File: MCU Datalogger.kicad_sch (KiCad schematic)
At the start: 0 parts

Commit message: Have added required symbols to the schematic sheets.
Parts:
- added BT?: Battery, symbol Device:Battery
- added C? (x4): C, symbol Device:C
- added C?: C_Polarized, symbol Device:C_Polarized
- added D? (x2): LED, symbol Device:LED
- added H? (x4): MountingHole, symbol Mechanical:MountingHole
- added R? (x7): R, symbol Device:R
- added U?: DS1337S+, SOIC127P600X175-8N, symbol DS1337S_:DS1337S+
- added U?: ATMEGA328P-AU, QFP80P900X900X120-32N, symbol ATMEGA328P-AU:ATMEGA328P-AU
- added U? (x2): 24LC1025, symbol Memory_EEPROM:24LC1025
- added Y? (x2): Crystal, symbol Device:Crystal
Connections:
- new net: U?.21 (GND), U?.3 (GND), U?.5 (GND)
- new net: U?.4 (VCC), U?.6 (VCC)
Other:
- added sheet Connectors (connectors.kicad_sch)

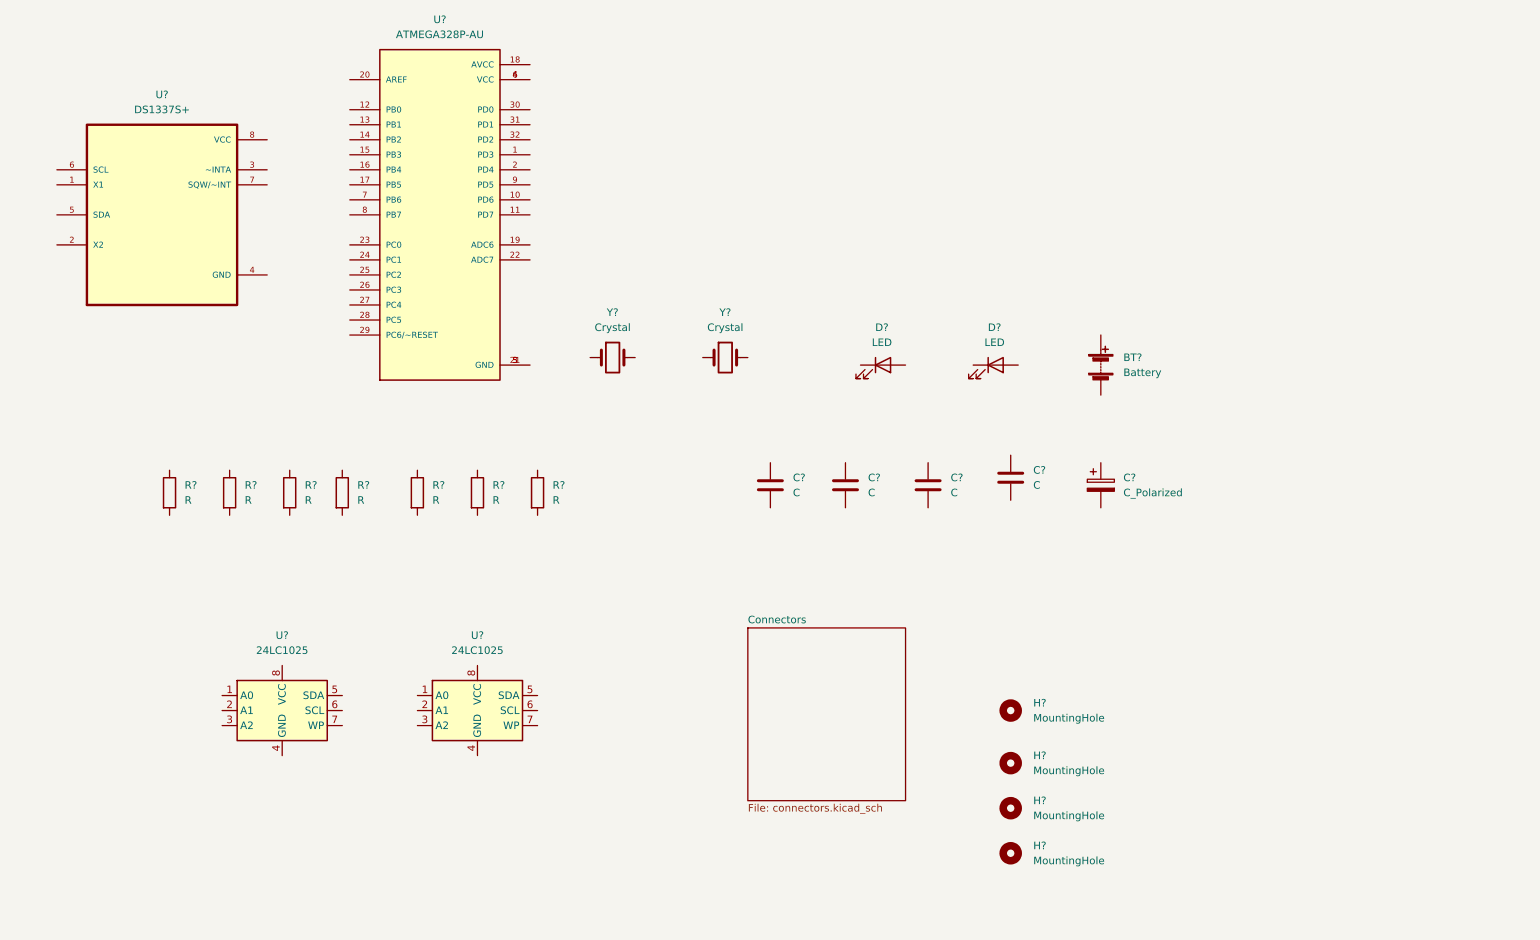
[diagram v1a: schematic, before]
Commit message: Changed locations of symbols (arrange).
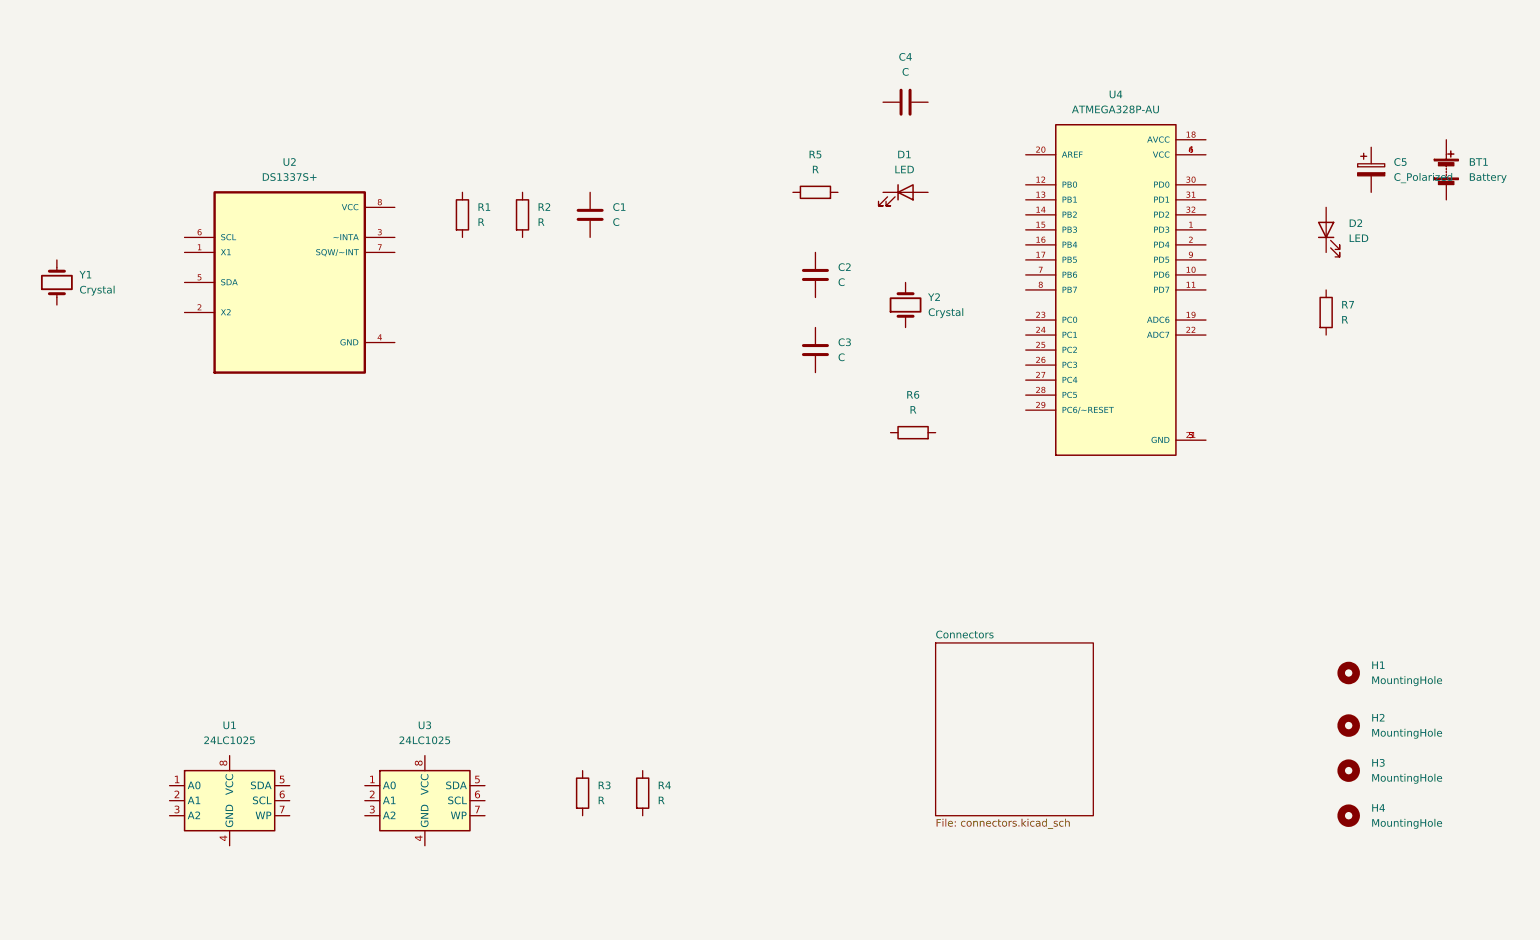
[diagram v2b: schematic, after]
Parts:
- gave numbers to parts that had none: 25
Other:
- moved on the sheet: BT1, C1, C2, C3, C4, C5, D1, D2, H1, H2, H3, H4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

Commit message: Added component values.
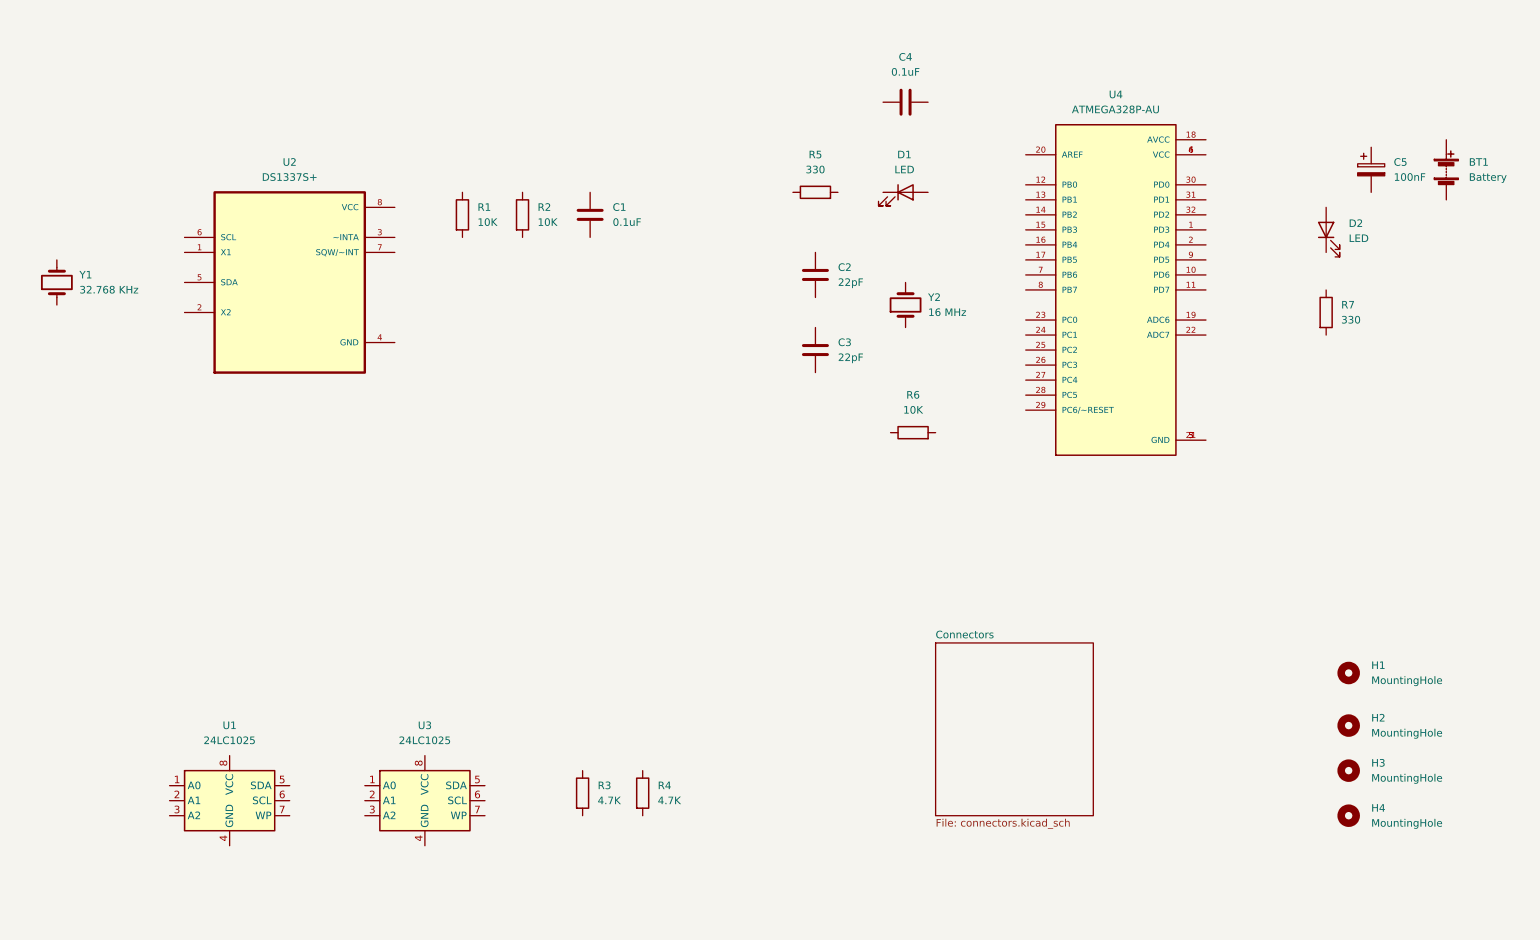
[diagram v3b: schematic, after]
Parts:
- C1, C4: value C -> 0.1uF
- C2, C3: value C -> 22pF
- C5: value C_Polarized -> 100nF
- R1, R2, R6: value R -> 10K
- R3, R4: value R -> 4.7K
- R5, R7: value R -> 330
- Y1: value Crystal -> 32.768 KHz
- Y2: value Crystal -> 16 MHz
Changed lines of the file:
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@@
       (effects (font (size 1.27 1.27)) (justify left))
     )
-    (property "Value" "R" (id 1) (at 99.06 52.0699 0)
+    (property "Value" "10K" (id 1) (at 99.06 52.0699 0)
       (effects (font (size 1.27 1.27)) (justify left))
     )
@@
       (effects (font (size 1.27 1.27)) (justify left))
     )
-    (property "Value" "R" (id 1) (at 109.22 52.0699 0)
+    (property "Value" "10K" (id 1) (at 109.22 52.0699 0)
       (effects (font (size 1.27 1.27)) (justify left))
     )
@@
       (effects (font (size 1.27 1.27)) (justify left))
     )
-    (property "Value" "R" (id 1) (at 119.38 149.8599 0)
+    (property "Value" "4.7K" (id 1) (at 119.38 149.8599 0)
       (effects (font (size 1.27 1.27)) (justify left))
     )
@@
       (effects (font (size 1.27 1.27)) (justify left))
     )
-    (property "Value" "R" (id 1) (at 129.54 149.8599 0)
+    (property "Value" "4.7K" (id 1) (at 129.54 149.8599 0)
       (effects (font (size 1.27 1.27)) (justify left))
     )
@@
     (in_bom yes) (on_board yes) (fields_autoplaced)
     (property "Reference" "R5" (id 0) (at 156.21 40.64 90))
-    (property "Value" "R" (id 1) (at 156.21 43.18 90))
+    (property "Value" "330" (id 1) (at 156.21 43.18 90))
     (property "Footprint" "" (id 2) (at 156.21 48.768 90)
       (effects (font (size 1.27 1.27)) hide)
@@
     (in_bom yes) (on_board yes) (fields_autoplaced)
     (property "Reference" "R6" (id 0) (at 172.72 81.28 90))
-    (property "Value" "R" (id 1) (at 172.72 83.82 90))
+    (property "Value" "10K" (id 1) (at 172.72 83.82 90))
     (property "Footprint" "" (id 2) (at 172.72 89.408 90)
       (effects (font (size 1.27 1.27)) hide)
@@
       (effects (font (size 1.27 1.27)) (justify left))
     )
-    (property "Value" "R" (id 1) (at 245.11 68.5799 0)
+    (property "Value" "330" (id 1) (at 245.11 68.5799 0)
       (effects (font (size 1.27 1.27)) (justify left))
     )
@@
       (effects (font (size 1.27 1.27)) (justify left))
     )
-    (property "Value" "C" (id 1) (at 121.92 52.0699 0)
+    (property "Value" "0.1uF" (id 1) (at 121.92 52.0699 0)
       (effects (font (size 1.27 1.27)) (justify left))
     )
@@
       (effects (font (size 1.27 1.27)) (justify left))
     )
-    (property "Value" "C" (id 1) (at 160.02 62.2299 0)
+    (property "Value" "22pF" (id 1) (at 160.02 62.2299 0)
       (effects (font (size 1.27 1.27)) (justify left))
     )
@@
       (effects (font (size 1.27 1.27)) (justify left))
     )
-    (property "Value" "C" (id 1) (at 160.02 74.9299 0)
+    (property "Value" "22pF" (id 1) (at 160.02 74.9299 0)
       (effects (font (size 1.27 1.27)) (justify left))
     )
@@
     (in_bom yes) (on_board yes) (fields_autoplaced)
     (property "Reference" "C4" (id 0) (at 171.45 24.13 90))
-    (property "Value" "C" (id 1) (at 171.45 26.67 90))
+    (property "Value" "0.1uF" (id 1) (at 171.45 26.67 90))
     (property "Footprint" "" (id 2) (at 175.26 30.7848 0)
       (effects (font (size 1.27 1.27)) hide)
@@
       (effects (font (size 1.27 1.27)) (justify left))
     )
-    (property "Value" "C_Polarized" (id 1) (at 254 44.4499 0)
+    (property "Value" "100nF" (id 1) (at 254 44.4499 0)
       (effects (font (size 1.27 1.27)) (justify left))
     )
@@
       (effects (font (size 1.27 1.27)) (justify right))
     )
-    (property "Value" "Crystal" (id 1) (at 31.75 63.4999 90)
+    (property "Value" "32.768 KHz" (id 1) (at 31.75 63.4999 90)
       (effects (font (size 1.27 1.27)) (justify right))
     )
@@
       (effects (font (size 1.27 1.27)) (justify right))
     )
-    (property "Value" "Crystal" (id 1) (at 175.26 67.3099 90)
+    (property "Value" "16 MHz" (id 1) (at 175.26 67.3099 90)
       (effects (font (size 1.27 1.27)) (justify right))
     )
@@
     )
     (path "/6297028a-be71-4f20-91c8-82bcaff02548"
-      (reference "C1") (unit 1) (value "C") (footprint "")
+      (reference "C1") (unit 1) (value "0.1uF") (footprint "")
     )
     (path "/b20b651d-5224-4b1d-8058-dedf55548381"
-      (reference "C2") (unit 1) (value "C") (footprint "")
+      (reference "C2") (unit 1) (value "22pF") (footprint "")
     )
     (path "/61e91196-d43d-4b19-ad57-2569feed4c9f"
-      (reference "C3") (unit 1) (value "C") (footprint "")
+      (reference "C3") (unit 1) (value "22pF") (footprint "")
     )
     (path "/e18320b2-42ab-4621-9e66-aee24e50ee4d"
-      (reference "C4") (unit 1) (value "C") (footprint "")
+      (reference "C4") (unit 1) (value "0.1uF") (footprint "")
     )
     (path "/9848e6a5-7312-4f8c-92b1-3add5171e047"
-      (reference "C5") (unit 1) (value "C_Polarized") (footprint "")
+      (reference "C5") (unit 1) (value "100nF") (footprint "")
     )
     (path "/1eeadbfa-9150-41d9-a500-dcf136c35db9"
@@
     )
     (path "/97ac78bd-d25a-4888-83fe-f9e71a972cd4"
-      (reference "R1") (unit 1) (value "R") (footprint "")
+      (reference "R1") (unit 1) (value "10K") (footprint "")
     )
     (path "/ab0dab26-12e7-4e58-b019-8e4a0c6725c0"
-      (reference "R2") (unit 1) (value "R") (footprint "")
+      (reference "R2") (unit 1) (value "10K") (footprint "")
     )
     (path "/1fd7d49c-0582-4c14-94ff-54e1705993d2"
-      (reference "R3") (unit 1) (value "R") (footprint "")
+      (reference "R3") (unit 1) (value "4.7K") (footprint "")
     )
     (path "/b45f5a9f-278e-4a8d-8551-d9db4c6a1ec1"
-      (reference "R4") (unit 1) (value "R") (footprint "")
+      (reference "R4") (unit 1) (value "4.7K") (footprint "")
     )
     (path "/d391bf22-eef6-425c-acb1-ca163f8377dd"
-      (reference "R5") (unit 1) (value "R") (footprint "")
+      (reference "R5") (unit 1) (value "330") (footprint "")
     )
     (path "/742f3083-6884-4bae-ab12-cdc4ace30719"
-      (reference "R6") (unit 1) (value "R") (footprint "")
+      (reference "R6") (unit 1) (value "10K") (footprint "")
     )
     (path "/00f3cdef-f95e-4809-a766-c9e14053963d"
-      (reference "R7") (unit 1) (value "R") (footprint "")
+      (reference "R7") (unit 1) (value "330") (footprint "")
     )
     (path "/ebdf0c6d-51a9-4fd0-b86d-b836acb8fabb"
@@
     )
     (path "/7a23f1ba-988a-49ab-b325-1b5495f21ba2"
-      (reference "Y1") (unit 1) (value "Crystal") (footprint "")
+      (reference "Y1") (unit 1) (value "32.768 KHz") (footprint "")
     )
     (path "/e2ccecb5-b706-4f55-8c55-b9e63717bc6e"
-      (reference "Y2") (unit 1) (value "Crystal") (footprint "")
-    )
-  )
+      (reference "Y2") (unit 1) (value "16 MHz") (footprint "")
+    )
+  )

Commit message: Completed symbol-footprint associations.
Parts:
- BT1: footprint (none) -> Connector_PinHeader_2.54mm:PinHeader_1x02_P2.54mm_Vertical
- C1, C2, C3, C4, C5: footprint (none) -> Capacitor_SMD:C_0805_2012Metric
- D1, D2: footprint (none) -> LED_SMD:LED_0805_2012Metric
- H1, H2, H3, H4: footprint (none) -> MountingHole:MountingHole_2.1mm
- R1, R2, R3, R4, R5, R6, R7: footprint (none) -> Resistor_SMD:R_0805_2012Metric
- U1, U3: footprint (none) -> Package_SO:SOIC-8_5.23x5.23mm_P1.27mm
- U2: footprint SOIC127P600X175-8N -> Footprints:SOIC127P600X175-8N
- U4: footprint QFP80P900X900X120-32N -> Footprints:QFP80P900X900X120-32N
- Y1, Y2: footprint (none) -> Crystal:Crystal_SMD_5032-2Pin_5.0x3.2mm_HandSoldering
